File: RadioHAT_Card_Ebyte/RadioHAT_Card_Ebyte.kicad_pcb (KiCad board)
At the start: 2 copper layers, 30 x 50.9 mm, 9 parts

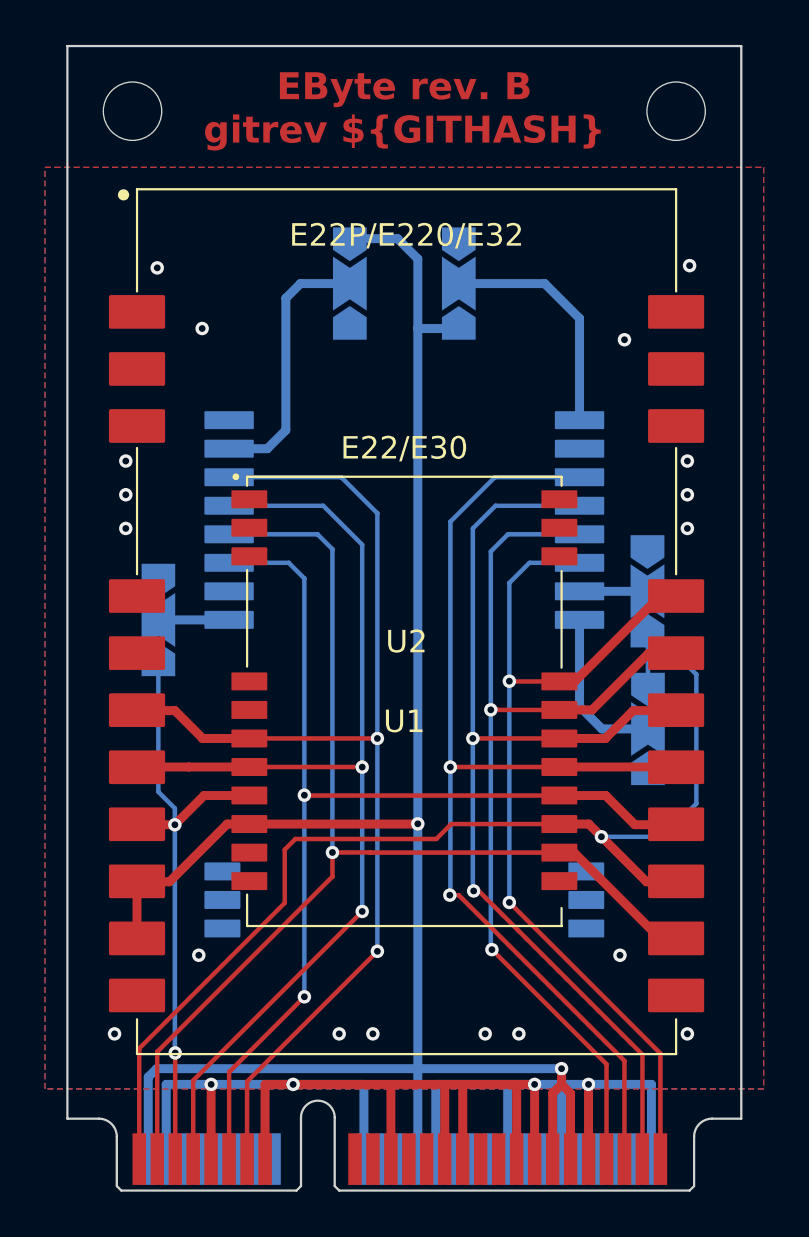
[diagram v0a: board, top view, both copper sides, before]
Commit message: [PCB] Cleanup traces
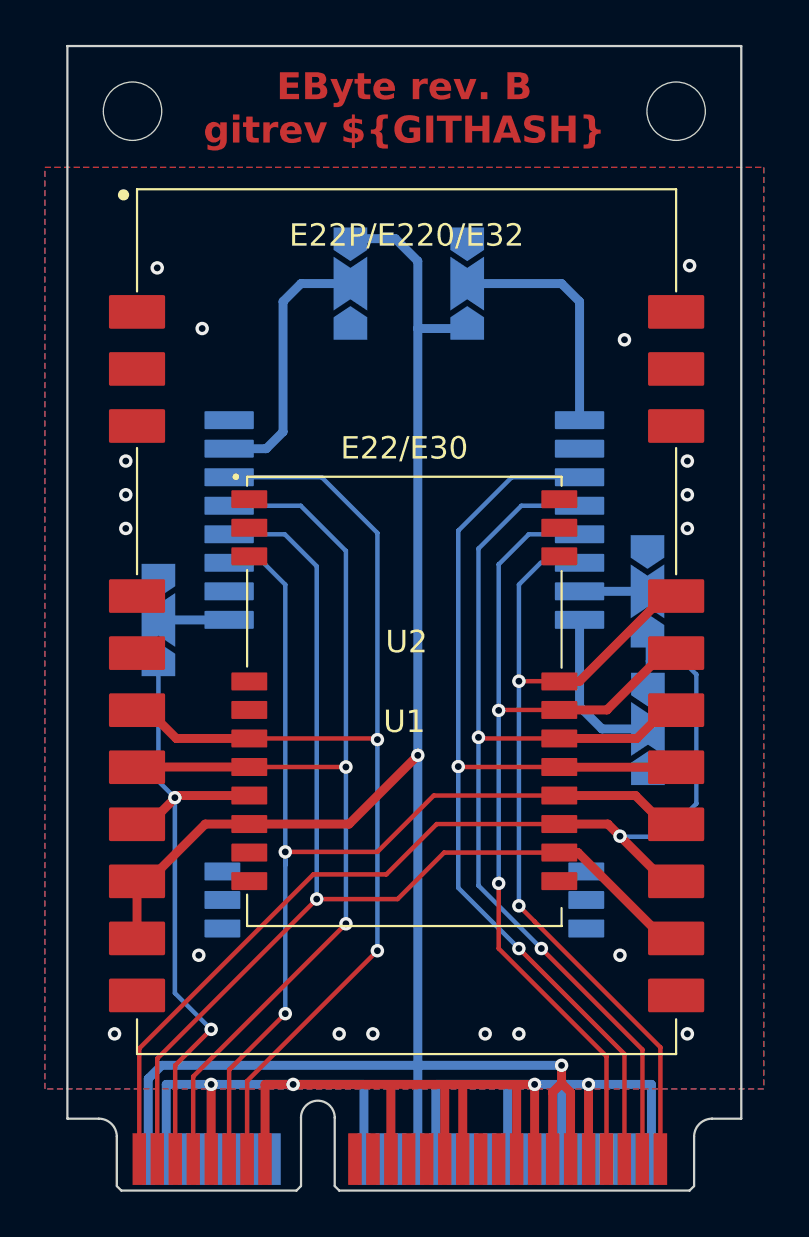
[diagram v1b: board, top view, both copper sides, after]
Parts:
- moved JP2 0.38 mm to (141.2, 94.6)
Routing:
- net RST0: track 48.0 -> 50.1 mm
- net GPIO1: track 47.2 -> 45.2 mm
- net GPIO0: track 50.6 -> 48.8 mm
- net +3V3: track 91.3 -> 93.1 mm
- net IRQ1: track 28.0 -> 29.7 mm
- net MISO: track 48.5 -> 47.2 mm
- net MOSI: track 46.1 -> 44.8 mm
- net SCK: track 42.7 -> 41.6 mm
- net NSS: track 41.6 -> 40.6 mm

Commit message: Update symbols to align with library
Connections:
- J1 pad 20: (no net) -> unconnected-(J1-NSS1-Pad20)
- J1 pad 28: (no net) -> unconnected-(J1-5V-Pad28)
- J1 pad 48: (no net) -> unconnected-(J1-5V-Pad48)
- J1 pad 6: (no net) -> unconnected-(J1-5V-Pad6)
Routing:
- net RST0: track 50.1 -> 49.1 mm
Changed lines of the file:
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@@
 	(net 30 "Net-(JP4-C)")
 	(net 31 "Net-(JP5-C)")
+	(net 32 "unconnected-(J1-5V-Pad48)")
+	(net 33 "unconnected-(J1-5V-Pad28)")
+	(net 34 "unconnected-(J1-NSS1-Pad20)")
+	(net 35 "unconnected-(J1-5V-Pad6)")
 	(footprint "RadioHAT:E22_Large"
 		(layer "F.Cu")
@@
 			)
 		)
+		(property "Mouser" "571-1775838-2"
+			(at 0 0 0)
+			(unlocked yes)
+			(layer "F.Fab")
+			(hide yes)
+			(effects
+				(font
+					(size 1 1)
+					(thickness 0.15)
+				)
+			)
+		)
 		(sheetname "/")
 		(sheetfile "RadioHAT_Card_Ebyte.kicad_sch")
@@
 			(size 2.3 0.6)
 			(layers "B.Cu" "B.Mask" "B.Paste")
+			(net 35 "unconnected-(J1-5V-Pad6)")
+			(pinfunction "5V")
+			(pintype "power_in+no_connect")
 			(thermal_bridge_angle 0)
 		)
@@
 			(size 2.3 0.6)
 			(layers "B.Cu" "B.Mask" "B.Paste")
+			(net 34 "unconnected-(J1-NSS1-Pad20)")
+			(pinfunction "NSS1")
+			(pintype "bidirectional+no_connect")
 			(thermal_bridge_angle 0)
 		)
@@
 			(size 2.3 0.6)
 			(layers "B.Cu" "B.Mask" "B.Paste")
+			(net 33 "unconnected-(J1-5V-Pad28)")
+			(pinfunction "5V")
+			(pintype "power_in+no_connect")
 			(thermal_bridge_angle 0)
 		)
@@
 			(size 2.3 0.6)
 			(layers "B.Cu" "B.Mask" "B.Paste")
+			(net 32 "unconnected-(J1-5V-Pad48)")
+			(pinfunction "5V")
+			(pintype "power_in+no_connect")
 			(thermal_bridge_angle 0)
 		)
@@
 			(layers "F.Cu" "F.Mask" "F.Paste")
 			(net 20 "NSS")
-			(pinfunction "SPI_NSS")
+			(pinfunction "NSS0")
 			(pintype "bidirectional")
 			(thermal_bridge_angle 0)
@@
 			(roundrect_rratio 0.05)
 			(net 3 "IRQ0")
-			(pinfunction "DIO9")
+			(pinfunction "DIO9/BUSY")
 			(pintype "bidirectional")
 			(thermal_bridge_angle 0)
@@
 			(roundrect_rratio 0.05)
 			(net 11 "GPIO1")
-			(pinfunction "DIO8")
+			(pinfunction "DIO8/DIO1")
 			(pintype "bidirectional")
 			(thermal_bridge_angle 0)
@@
 			(roundrect_rratio 0.05)
 			(net 6 "RST1")
-			(pinfunction "DIO7")
+			(pinfunction "DIO7/DIO2")
 			(pintype "bidirectional")
 			(thermal_bridge_angle 0)
@@
 	)
 	(segment
-		(start 133.1 119.9)
-		(end 133.1 120.5)
+		(start 133.1 127.1)
+		(end 133.1 119.9)
 		(width 0.2)
 		(layer "B.Cu")
@@
 	)
 	(segment
-		(start 133.1 119.9)
-		(end 133.1 120.3)
-		(width 0.2)
-		(layer "B.Cu")
-		(net 16)
-	)
-	(segment
 		(start 133.1 108)
 		(end 132.13 107.03)
 		(width 0.2)
 		(layer "B.Cu")
-		(net 16)
-	)
-	(segment
-		(start 133.1 127.1)
-		(end 133.1 119.9)
-		(width 0.2)
-		(layer "B.Cu")
